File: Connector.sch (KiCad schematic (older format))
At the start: 4 parts

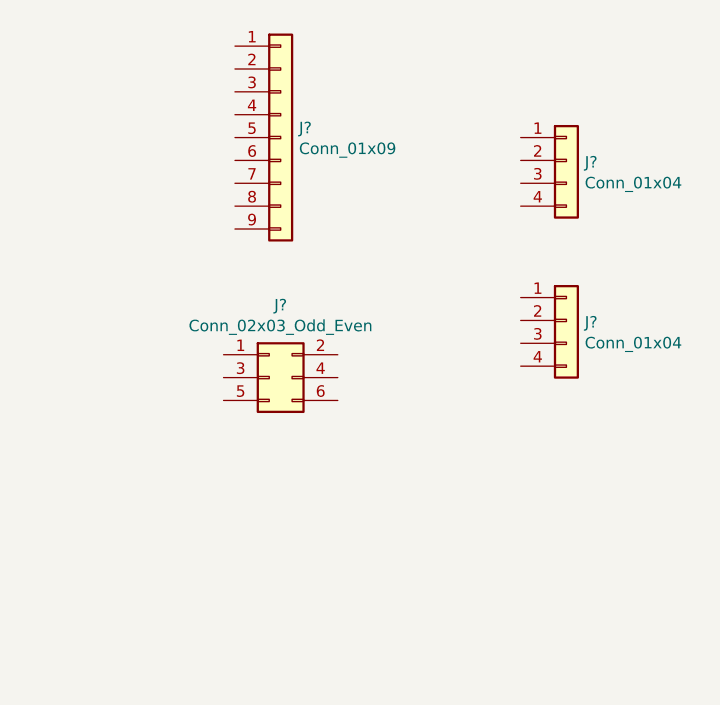
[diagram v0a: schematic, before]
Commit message: Added missing symbols, arranged symbols, annotated.
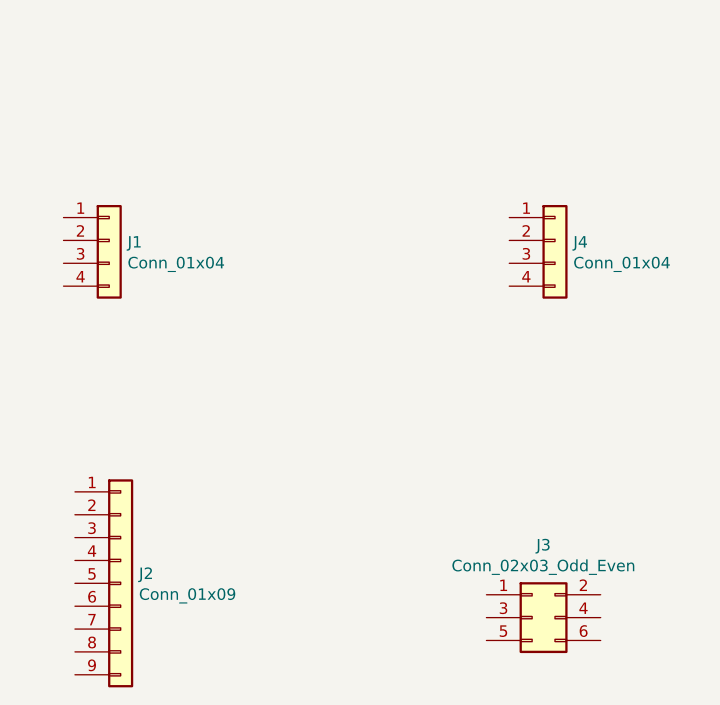
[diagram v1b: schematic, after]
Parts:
- gave numbers to parts that had none: 4
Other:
- moved on the sheet: J1, J2, J3, J4
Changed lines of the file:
@@
 $EndDescr
 $Comp
-L Connector_Generic:Conn_01x09 J?
+L Connector_Generic:Conn_01x09 J2
 U 1 1 5CF96448
-P 5400 3150
-F 0 "J?" H 5480 3192 50  0000 L CNN
-F 1 "Conn_01x09" H 5480 3101 50  0000 L CNN
-F 2 "" H 5400 3150 50  0001 C CNN
-F 3 "~" H 5400 3150 50  0001 C CNN
-	1    5400 3150
+P 4700 5100
+F 0 "J2" H 4780 5142 50  0000 L CNN
+F 1 "Conn_01x09" H 4780 5051 50  0000 L CNN
+F 2 "" H 4700 5100 50  0001 C CNN
+F 3 "~" H 4700 5100 50  0001 C CNN
+	1    4700 5100
 	1    0    0    -1
 $EndComp
 $Comp
-L Connector_Generic:Conn_01x04 J?
+L Connector_Generic:Conn_01x04 J1
 U 1 1 5CF96B03
-P 6650 3250
-F 0 "J?" H 6730 3242 50  0000 L CNN
-F 1 "Conn_01x04" H 6730 3151 50  0000 L CNN
-F 2 "" H 6650 3250 50  0001 C CNN
-F 3 "~" H 6650 3250 50  0001 C CNN
-	1    6650 3250
+P 4650 3600
+F 0 "J1" H 4730 3592 50  0000 L CNN
+F 1 "Conn_01x04" H 4730 3501 50  0000 L CNN
+F 2 "" H 4650 3600 50  0001 C CNN
+F 3 "~" H 4650 3600 50  0001 C CNN
+	1    4650 3600
 	1    0    0    -1
 $EndComp
 $Comp
-L Connector_Generic:Conn_02x03_Odd_Even J?
+L Connector_Generic:Conn_02x03_Odd_Even J3
 U 1 1 5CF9727B
-P 5350 4200
-F 0 "J?" H 5400 4517 50  0000 C CNN
-F 1 "Conn_02x03_Odd_Even" H 5400 4426 50  0000 C CNN
-F 2 "" H 5350 4200 50  0001 C CNN
-F 3 "~" H 5350 4200 50  0001 C CNN
-	1    5350 4200
+P 6500 5250
+F 0 "J3" H 6550 5567 50  0000 C CNN
+F 1 "Conn_02x03_Odd_Even" H 6550 5476 50  0000 C CNN
+F 2 "" H 6500 5250 50  0001 C CNN
+F 3 "~" H 6500 5250 50  0001 C CNN
+	1    6500 5250
 	1    0    0    -1
 $EndComp
 $Comp
-L Connector_Generic:Conn_01x04 J?
+L Connector_Generic:Conn_01x04 J4
 U 1 1 5CF97B22
-P 6650 3950
-F 0 "J?" H 6730 3942 50  0000 L CNN
-F 1 "Conn_01x04" H 6730 3851 50  0000 L CNN
-F 2 "" H 6650 3950 50  0001 C CNN
-F 3 "~" H 6650 3950 50  0001 C CNN
-	1    6650 3950
+P 6600 3600
+F 0 "J4" H 6680 3592 50  0000 L CNN
+F 1 "Conn_01x04" H 6680 3501 50  0000 L CNN
+F 2 "" H 6600 3600 50  0001 C CNN
+F 3 "~" H 6600 3600 50  0001 C CNN
+	1    6600 3600
 	1    0    0    -1
 $EndComp

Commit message: Completed associations and added component values.
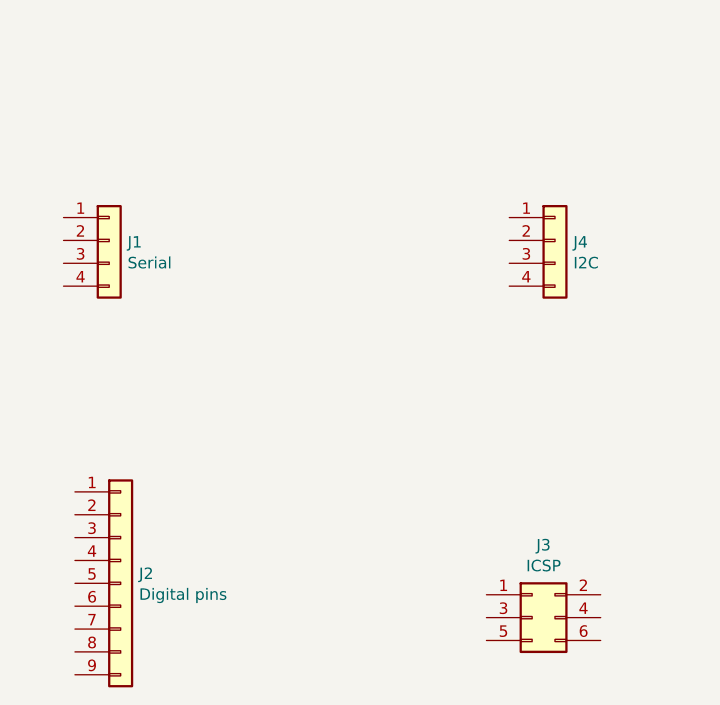
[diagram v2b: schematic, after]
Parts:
- J1: value Conn_01x04 -> Serial; footprint (none) -> Connector_PinHeader_2.54mm:PinHeader_1x04_P2.54mm_Vertical
- J2: value Conn_01x09 -> Digital pins; footprint (none) -> Connector_PinHeader_2.54mm:PinHeader_1x09_P2.54mm_Vertical
- J3: value Conn_02x03_Odd_Even -> ICSP; footprint (none) -> Connector_PinSocket_2.54mm:PinSocket_2x03_P2.54mm_Vertical
- J4: value Conn_01x04 -> I2C; footprint (none) -> Connector_PinSocket_2.54mm:PinSocket_1x04_P2.54mm_Vertical
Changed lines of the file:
@@
 P 4700 5100
 F 0 "J2" H 4780 5142 50  0000 L CNN
-F 1 "Conn_01x09" H 4780 5051 50  0000 L CNN
-F 2 "" H 4700 5100 50  0001 C CNN
+F 1 "Digital pins" H 4780 5051 50  0000 L CNN
+F 2 "Connector_PinHeader_2.54mm:PinHeader_1x09_P2.54mm_Vertical" H 4700 5100 50  0001 C CNN
 F 3 "~" H 4700 5100 50  0001 C CNN
 	1    4700 5100
@@
 P 4650 3600
 F 0 "J1" H 4730 3592 50  0000 L CNN
-F 1 "Conn_01x04" H 4730 3501 50  0000 L CNN
-F 2 "" H 4650 3600 50  0001 C CNN
+F 1 "Serial" H 4730 3501 50  0000 L CNN
+F 2 "Connector_PinHeader_2.54mm:PinHeader_1x04_P2.54mm_Vertical" H 4650 3600 50  0001 C CNN
 F 3 "~" H 4650 3600 50  0001 C CNN
 	1    4650 3600
@@
 P 6500 5250
 F 0 "J3" H 6550 5567 50  0000 C CNN
-F 1 "Conn_02x03_Odd_Even" H 6550 5476 50  0000 C CNN
-F 2 "" H 6500 5250 50  0001 C CNN
+F 1 "ICSP" H 6550 5476 50  0000 C CNN
+F 2 "Connector_PinSocket_2.54mm:PinSocket_2x03_P2.54mm_Vertical" H 6500 5250 50  0001 C CNN
 F 3 "~" H 6500 5250 50  0001 C CNN
 	1    6500 5250
@@
 P 6600 3600
 F 0 "J4" H 6680 3592 50  0000 L CNN
-F 1 "Conn_01x04" H 6680 3501 50  0000 L CNN
-F 2 "" H 6600 3600 50  0001 C CNN
+F 1 "I2C" H 6680 3501 50  0000 L CNN
+F 2 "Connector_PinSocket_2.54mm:PinSocket_1x04_P2.54mm_Vertical" H 6600 3600 50  0001 C CNN
 F 3 "~" H 6600 3600 50  0001 C CNN
 	1    6600 3600

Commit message: Completed wiring in the connectors sheet.
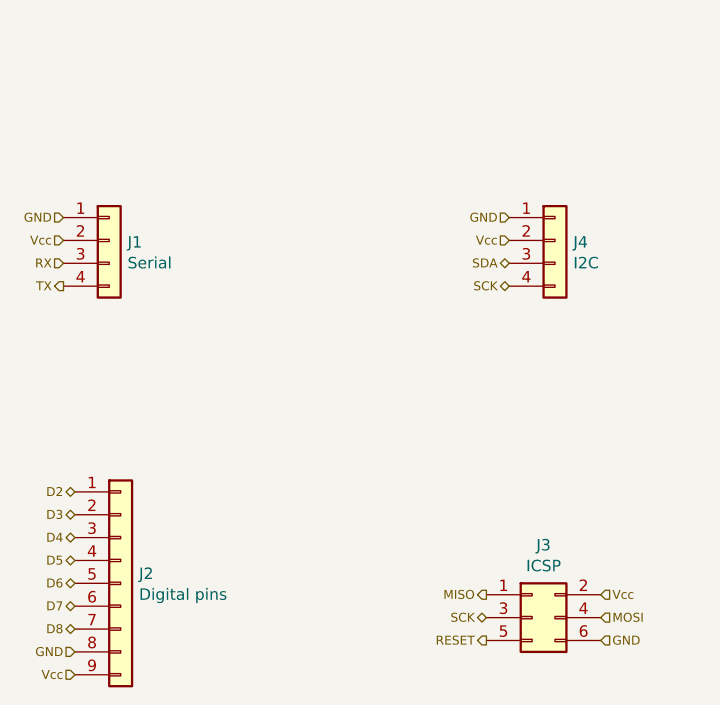
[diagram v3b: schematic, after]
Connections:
- net D2: now reaches J2.1 (Pin_1)
- net D3: now reaches J2.2 (Pin_2)
- net D4: now reaches J2.3 (Pin_3)
- net D5: now reaches J2.4 (Pin_4)
- net D6: now reaches J2.5 (Pin_5)
- net D7: now reaches J2.6 (Pin_6)
- net D8: now reaches J2.7 (Pin_7)
- net GND: now reaches J2.8 (Pin_8)
- net GND: now also J1.1 (Pin_1), J3.6 (Pin_6), J4.1 (Pin_1)
- net Vcc: now reaches J2.9 (Pin_9)
- net Vcc: now also J1.2 (Pin_2), J3.2 (Pin_2), J4.2 (Pin_2)
- net RX: now reaches J1.3 (Pin_3)
- net TX: now reaches J1.4 (Pin_4)
- net MISO: now reaches J3.1 (Pin_1)
- net SCK: now reaches J3.3 (Pin_3)
- net SCK: now also J4.4 (Pin_4)
- net MOSI: now reaches J3.4 (Pin_4)
- net RESET: now reaches J3.5 (Pin_5)
- net SDA: now reaches J4.3 (Pin_3)
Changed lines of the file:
@@
 	1    0    0    -1
 $EndComp
+Text HLabel 6300 5150 0    39   Output ~ 0
+MISO
+Text HLabel 6300 5250 0    39   BiDi ~ 0
+SCK
+Text HLabel 6300 5350 0    39   Output ~ 0
+RESET
+Text HLabel 6800 5150 2    39   Input ~ 0
+Vcc
+Text HLabel 6800 5250 2    39   Input ~ 0
+MOSI
+Text HLabel 6800 5350 2    39   Input ~ 0
+GND
+Text HLabel 4450 3500 0    39   Input ~ 0
+GND
+Text HLabel 4450 3600 0    39   Input ~ 0
+Vcc
+Text HLabel 4450 3700 0    39   Input ~ 0
+RX
+Text HLabel 4450 3800 0    39   Output ~ 0
+TX
+Text HLabel 6400 3500 0    39   Input ~ 0
+GND
+Text HLabel 6400 3600 0    39   Input ~ 0
+Vcc
+Text HLabel 6400 3700 0    39   BiDi ~ 0
+SDA
+Text HLabel 6400 3800 0    39   BiDi ~ 0
+SCK
+Text HLabel 4500 4700 0    39   BiDi ~ 0
+D2
+Text HLabel 4500 4800 0    39   BiDi ~ 0
+D3
+Text HLabel 4500 4900 0    39   BiDi ~ 0
+D4
+Text HLabel 4500 5000 0    39   BiDi ~ 0
+D5
+Text HLabel 4500 5100 0    39   BiDi ~ 0
+D6
+Text HLabel 4500 5200 0    39   BiDi ~ 0
+D7
+Text HLabel 4500 5300 0    39   BiDi ~ 0
+D8
+Text HLabel 4500 5400 0    39   Input ~ 0
+GND
+Text HLabel 4500 5500 0    39   Input ~ 0
+Vcc
 $EndSCHEMATC

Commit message: Added functional block descriptions.
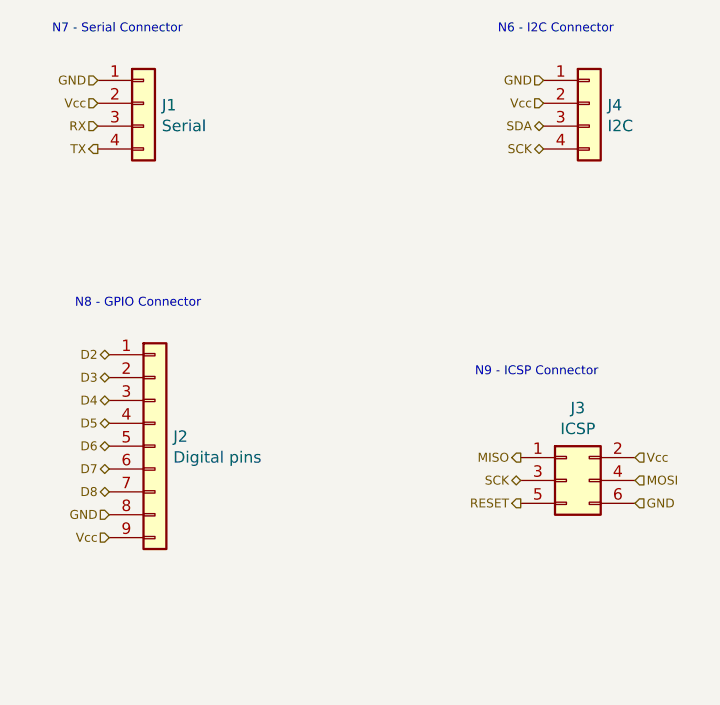
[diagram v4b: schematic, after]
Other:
- note added: "N6 - I2C Connector"
- note added: "N7 - Serial Connector"
- note added: "N8 - GPIO Connector"
- note added: "N9 - ICSP Connector"
- moved on the sheet: J1, J2, J3, J4
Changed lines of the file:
@@
 L Connector_Generic:Conn_01x09 J2
 U 1 1 5CF96448
-P 4700 5100
-F 0 "J2" H 4780 5142 50  0000 L CNN
-F 1 "Digital pins" H 4780 5051 50  0000 L CNN
-F 2 "Connector_PinHeader_2.54mm:PinHeader_1x09_P2.54mm_Vertical" H 4700 5100 50  0001 C CNN
-F 3 "~" H 4700 5100 50  0001 C CNN
-	1    4700 5100
+P 4850 4500
+F 0 "J2" H 4930 4542 50  0000 L CNN
+F 1 "Digital pins" H 4930 4451 50  0000 L CNN
+F 2 "Connector_PinHeader_2.54mm:PinHeader_1x09_P2.54mm_Vertical" H 4850 4500 50  0001 C CNN
+F 3 "~" H 4850 4500 50  0001 C CNN
+	1    4850 4500
 	1    0    0    -1
 $EndComp
@@
 L Connector_Generic:Conn_01x04 J1
 U 1 1 5CF96B03
-P 4650 3600
-F 0 "J1" H 4730 3592 50  0000 L CNN
-F 1 "Serial" H 4730 3501 50  0000 L CNN
-F 2 "Connector_PinHeader_2.54mm:PinHeader_1x04_P2.54mm_Vertical" H 4650 3600 50  0001 C CNN
-F 3 "~" H 4650 3600 50  0001 C CNN
-	1    4650 3600
+P 4800 3000
+F 0 "J1" H 4880 2992 50  0000 L CNN
+F 1 "Serial" H 4880 2901 50  0000 L CNN
+F 2 "Connector_PinHeader_2.54mm:PinHeader_1x04_P2.54mm_Vertical" H 4800 3000 50  0001 C CNN
+F 3 "~" H 4800 3000 50  0001 C CNN
+	1    4800 3000
 	1    0    0    -1
 $EndComp
@@
 L Connector_Generic:Conn_02x03_Odd_Even J3
 U 1 1 5CF9727B
-P 6500 5250
-F 0 "J3" H 6550 5567 50  0000 C CNN
-F 1 "ICSP" H 6550 5476 50  0000 C CNN
-F 2 "Connector_PinSocket_2.54mm:PinSocket_2x03_P2.54mm_Vertical" H 6500 5250 50  0001 C CNN
-F 3 "~" H 6500 5250 50  0001 C CNN
-	1    6500 5250
+P 6650 4650
+F 0 "J3" H 6700 4967 50  0000 C CNN
+F 1 "ICSP" H 6700 4876 50  0000 C CNN
+F 2 "Connector_PinSocket_2.54mm:PinSocket_2x03_P2.54mm_Vertical" H 6650 4650 50  0001 C CNN
+F 3 "~" H 6650 4650 50  0001 C CNN
+	1    6650 4650
 	1    0    0    -1
 $EndComp
@@
 L Connector_Generic:Conn_01x04 J4
 U 1 1 5CF97B22
-P 6600 3600
-F 0 "J4" H 6680 3592 50  0000 L CNN
-F 1 "I2C" H 6680 3501 50  0000 L CNN
-F 2 "Connector_PinSocket_2.54mm:PinSocket_1x04_P2.54mm_Vertical" H 6600 3600 50  0001 C CNN
-F 3 "~" H 6600 3600 50  0001 C CNN
-	1    6600 3600
+P 6750 3000
+F 0 "J4" H 6830 2992 50  0000 L CNN
+F 1 "I2C" H 6830 2901 50  0000 L CNN
+F 2 "Connector_PinSocket_2.54mm:PinSocket_1x04_P2.54mm_Vertical" H 6750 3000 50  0001 C CNN
+F 3 "~" H 6750 3000 50  0001 C CNN
+	1    6750 3000
 	1    0    0    -1
 $EndComp
-Text HLabel 6300 5150 0    39   Output ~ 0
+Text HLabel 6450 4550 0    39   Output ~ 0
 MISO
-Text HLabel 6300 5250 0    39   BiDi ~ 0
+Text HLabel 6450 4650 0    39   BiDi ~ 0
 SCK
-Text HLabel 6300 5350 0    39   Output ~ 0
+Text HLabel 6450 4750 0    39   Output ~ 0
 RESET
-Text HLabel 6800 5150 2    39   Input ~ 0
+Text HLabel 6950 4550 2    39   Input ~ 0
 Vcc
-Text HLabel 6800 5250 2    39   Input ~ 0
+Text HLabel 6950 4650 2    39   Input ~ 0
 MOSI
-Text HLabel 6800 5350 2    39   Input ~ 0
+Text HLabel 6950 4750 2    39   Input ~ 0
 GND
-Text HLabel 4450 3500 0    39   Input ~ 0
+Text HLabel 4600 2900 0    39   Input ~ 0
 GND
-Text HLabel 4450 3600 0    39   Input ~ 0
+Text HLabel 4600 3000 0    39   Input ~ 0
 Vcc
-Text HLabel 4450 3700 0    39   Input ~ 0
+Text HLabel 4600 3100 0    39   Input ~ 0
 RX
-Text HLabel 4450 3800 0    39   Output ~ 0
+Text HLabel 4600 3200 0    39   Output ~ 0
 TX
-Text HLabel 6400 3500 0    39   Input ~ 0
+Text HLabel 6550 2900 0    39   Input ~ 0
 GND
-Text HLabel 6400 3600 0    39   Input ~ 0
+Text HLabel 6550 3000 0    39   Input ~ 0
 Vcc
-Text HLabel 6400 3700 0    39   BiDi ~ 0
+Text HLabel 6550 3100 0    39   BiDi ~ 0
 SDA
-Text HLabel 6400 3800 0    39   BiDi ~ 0
+Text HLabel 6550 3200 0    39   BiDi ~ 0
 SCK
-Text HLabel 4500 4700 0    39   BiDi ~ 0
+Text HLabel 4650 4100 0    39   BiDi ~ 0
 D2
-Text HLabel 4500 4800 0    39   BiDi ~ 0
+Text HLabel 4650 4200 0    39   BiDi ~ 0
 D3
-Text HLabel 4500 4900 0    39   BiDi ~ 0
+Text HLabel 4650 4300 0    39   BiDi ~ 0
 D4
-Text HLabel 4500 5000 0    39   BiDi ~ 0
+Text HLabel 4650 4400 0    39   BiDi ~ 0
 D5
-Text HLabel 4500 5100 0    39   BiDi ~ 0
+Text HLabel 4650 4500 0    39   BiDi ~ 0
 D6
-Text HLabel 4500 5200 0    39   BiDi ~ 0
+Text HLabel 4650 4600 0    39   BiDi ~ 0
 D7
-Text HLabel 4500 5300 0    39   BiDi ~ 0
+Text HLabel 4650 4700 0    39   BiDi ~ 0
 D8
-Text HLabel 4500 5400 0    39   Input ~ 0
+Text HLabel 4650 4800 0    39   Input ~ 0
 GND
-Text HLabel 4500 5500 0    39   Input ~ 0
+Text HLabel 4650 4900 0    39   Input ~ 0
 Vcc
+Text Notes 6350 2700 0    39   ~ 0
+N6 - I2C Connector
+Text Notes 4400 2700 0    39   ~ 0
+N7 - Serial Connector
+Text Notes 4500 3900 0    39   ~ 0
+N8 - GPIO Connector
+Text Notes 6250 4200 0    39   ~ 0
+N9 - ICSP Connector
 $EndSCHEMATC
